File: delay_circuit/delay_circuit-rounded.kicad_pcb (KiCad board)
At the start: 2 copper layers, 133 x 90 mm, 26 parts, among them J1 IN 12V AC, J2 OUT 230V AC, J3 IN 230V AC, J4 From Trfo Output, J5 OUT 5V CC, J6 To Power Ampli Power IN, J7 From Ampli Output, J8 OUT 12V CC, J9 To Speakers, K1 SANYOU_SRD_Form_C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

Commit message: Improved PCB.
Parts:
- moved J9 8.33 mm to (86.0, 32.5)
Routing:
- net Net-(D2-K): track 100.1 -> 92.6 mm
- net Net-(J7-Pin_2): track 105.9 -> 101.0 mm
- net 12V GND: track 152.7 -> 157.5 mm
- net IN SP L+: track 70.3 -> 74.5 mm
- net OUT SP R+: track 69.4 -> 72.8 mm
- net 0: track 107.4 -> 104.0 mm
- net IN SP R+: track 41.6 -> 40.2 mm
- net Net-(J8-Pin_1): track 78.0 -> 76.6 mm
- net Net-(J1-Pin_1): track 23.1 -> 21.9 mm
- net Net-(Q1-E): track 24.0 -> 23.0 mm
- net Net-(J2-Pin_1): track 72.7 -> 71.7 mm
- net Net-(D1-+): track 54.4 -> 53.5 mm
- net Net-(J2-Pin_2): track 71.9 -> 71.3 mm
- net Net-(J5-Pin_2): track 43.8 -> 43.2 mm
- net OUT SP L+: track 77.7 -> 78.3 mm
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- added copper zone on B.Cu, net (none)
- added copper zone on B.Cu, net 0
- added copper zone on B.Cu, net 12V GND
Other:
- board size 133 x 90 mm -> 132 x 90 mm
- board text added: "5VDC OUT"
- board text removed: "5V DC OUT"

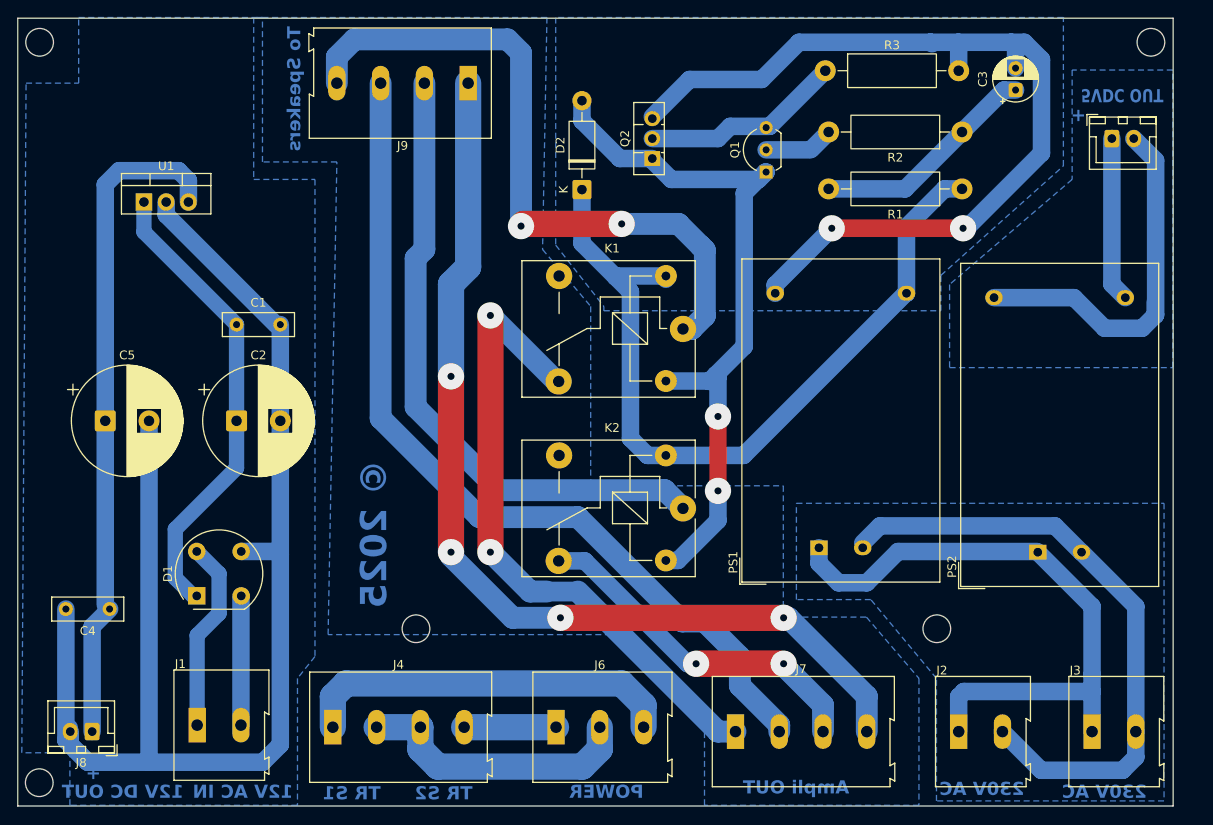
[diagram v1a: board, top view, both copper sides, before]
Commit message: Reduced board size.
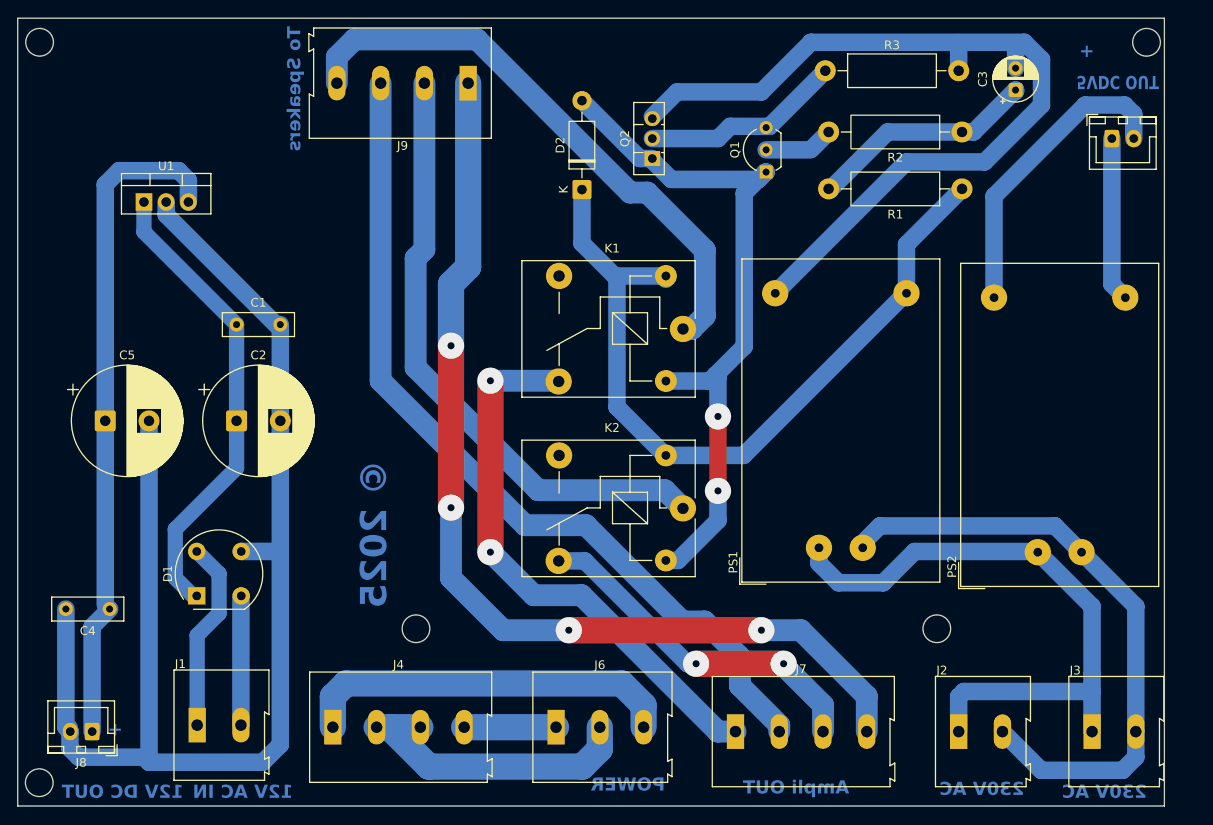
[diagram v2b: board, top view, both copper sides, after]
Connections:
- PS1 pad 3: 0 -> Net-(D2-K)
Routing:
- net OUT SP L+: track 78.3 -> 66.5 mm, vias 2 -> 0
- net IN SP L+: track 74.5 -> 63.9 mm
- net Net-(J5-Pin_2): track 43.2 -> 35.1 mm
- net 0: track 104.0 -> 99.2 mm, vias 2 -> 0
- net 12V GND: track 157.5 -> 153.5 mm
- net OUT SP R+: track 72.8 -> 70.1 mm
- net Net-(J7-Pin_2): track 101.0 -> 98.5 mm
- net Net-(D2-K): track 92.6 -> 90.3 mm
- net Net-(J4-Pin_2): track 32.2 -> 34.2 mm
- net Net-(J7-Pin_4): track 113.0 -> 114.5 mm
- net Net-(D2-A): track 82.6 -> 81.2 mm
- net Net-(J2-Pin_2): track 71.3 -> 70.7 mm
- removed copper zone on B.Cu, net (none)
- removed copper zone on B.Cu, net 0
- removed copper zone on B.Cu, net 12V GND
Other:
- board size 132 x 90 mm -> 131 x 90 mm
- board text removed: "TR S1"
- board text removed: "TR S2"
